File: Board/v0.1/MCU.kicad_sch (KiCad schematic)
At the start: 27 parts, among them J1 Conn_01x06_Male, SW1 RST_BTN, SW2 SCREEN_OFF_BTN, U1 ESP32-WROOM-32

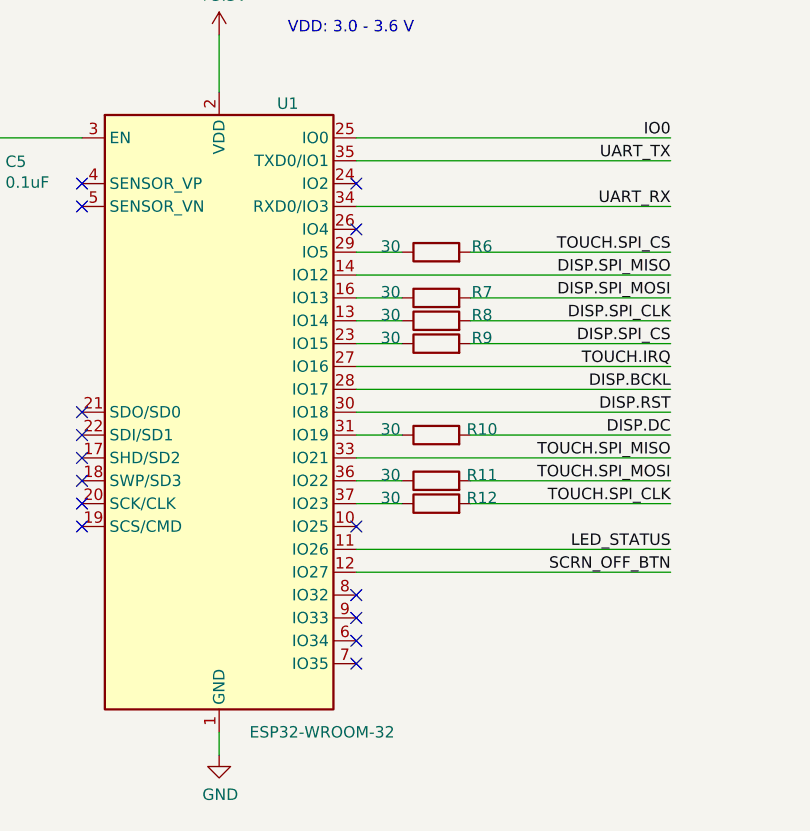
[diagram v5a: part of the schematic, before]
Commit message: Add labels to unused pins
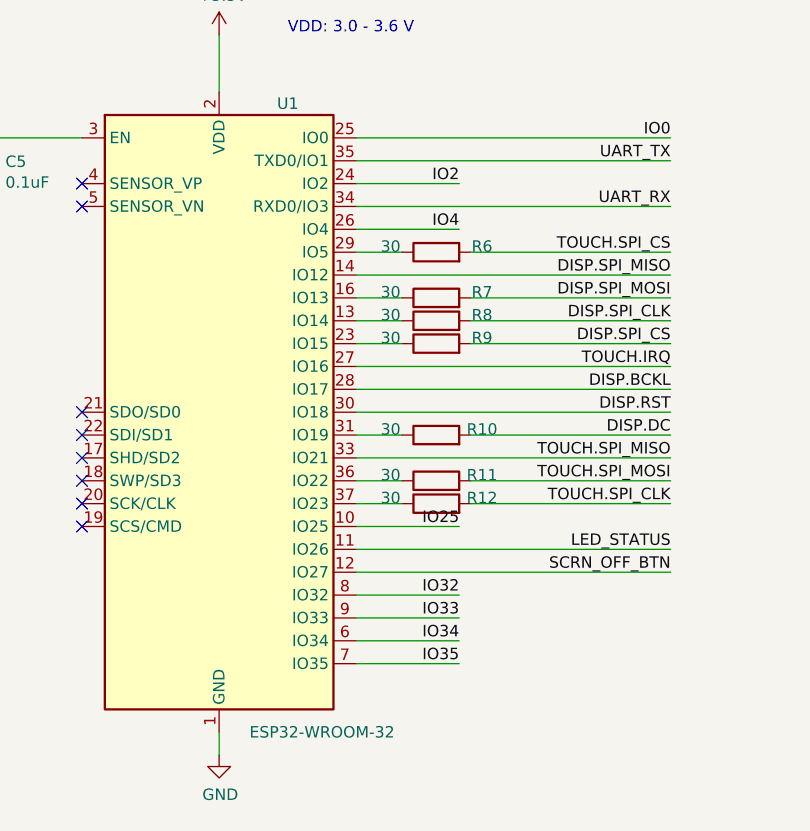
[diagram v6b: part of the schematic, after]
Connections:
- net IO25: now reaches U1.10 (IO25)
- net IO2: now reaches U1.24 (IO2)
- net IO4: now reaches U1.26 (IO4)
- net IO34: now reaches U1.6 (IO34)
- net IO35: now reaches U1.7 (IO35)
- net IO32: now reaches U1.8 (IO32)
- net IO33: now reaches U1.9 (IO33)
- no-connect marks 15 -> 8
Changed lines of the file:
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@@
   (no_connect (at 125.73 97.79))
   (no_connect (at 125.73 95.25))
-  (no_connect (at 156.21 115.57))
-  (no_connect (at 156.21 118.11))
   (no_connect (at 125.73 67.31))
-  (no_connect (at 156.21 113.03))
   (no_connect (at 125.73 100.33))
-  (no_connect (at 156.21 64.77))
-  (no_connect (at 156.21 102.87))
-  (no_connect (at 156.21 69.85))
   (no_connect (at 125.73 90.17))
   (no_connect (at 125.73 64.77))
   (no_connect (at 125.73 92.71))
-  (no_connect (at 156.21 110.49))
   (no_connect (at 125.73 102.87))
   (bus_entry (at 245.11 60.96) (size 2.54 2.54)
@@
     (stroke (width 0) (type default) (color 0 0 0 0))
   )
+  (wire (pts (xy 156.21 69.85) (xy 167.64 69.85))
+    (stroke (width 0) (type default) (color 0 0 0 0))
+  )
   (wire (pts (xy 99.06 59.69) (xy 104.14 59.69))
     (stroke (width 0) (type default) (color 0 0 0 0))
@@
     (stroke (width 0) (type default) (color 0 0 0 0))
   )
+  (wire (pts (xy 156.21 118.11) (xy 167.64 118.11))
+    (stroke (width 0) (type default) (color 0 0 0 0))
+  )
   (wire (pts (xy 228.6 63.5) (xy 245.11 63.5))
     (stroke (width 0) (type default) (color 0 0 0 0))
@@
     (stroke (width 0) (type default) (color 0 0 0 0))
   )
+  (wire (pts (xy 156.21 64.77) (xy 167.64 64.77))
+    (stroke (width 0) (type default) (color 0 0 0 0))
+  )
   (wire (pts (xy 60.96 177.8) (xy 60.96 179.705))
     (stroke (width 0) (type default) (color 0 0 0 0))
@@
     (stroke (width 0) (type default) (color 0 0 0 0))
   )
+  (wire (pts (xy 156.21 110.49) (xy 167.64 110.49))
+    (stroke (width 0) (type default) (color 0 0 0 0))
+  )
   (wire (pts (xy 156.21 80.01) (xy 161.29 80.01))
     (stroke (width 0) (type default) (color 0 0 0 0))
@@
     (stroke (width 0) (type default) (color 0 0 0 0))
   )
+  (wire (pts (xy 156.21 115.57) (xy 167.64 115.57))
+    (stroke (width 0) (type default) (color 0 0 0 0))
+  )
   (wire (pts (xy 268.605 147.955) (xy 261.62 147.955))
     (stroke (width 0) (type default) (color 0 0 0 0))
   )
+  (wire (pts (xy 156.21 113.03) (xy 167.64 113.03))
+    (stroke (width 0) (type default) (color 0 0 0 0))
+  )
   (wire (pts (xy 156.21 59.69) (xy 191.135 59.69))
     (stroke (width 0) (type default) (color 0 0 0 0))
@@
   )
   (wire (pts (xy 60.96 167.64) (xy 62.865 167.64))
+    (stroke (width 0) (type default) (color 0 0 0 0))
+  )
+  (wire (pts (xy 156.21 102.87) (xy 167.64 102.87))
     (stroke (width 0) (type default) (color 0 0 0 0))
   )
@@
     (effects (font (size 1.27 1.27)) (justify right bottom))
   )
+  (label "IO25" (at 167.64 102.87 180)
+    (effects (font (size 1.27 1.27)) (justify right bottom))
+  )
   (label "DISP.BCKL" (at 191.135 87.63 180)
     (effects (font (size 1.27 1.27)) (justify right bottom))
   )
+  (label "IO33" (at 167.64 113.03 180)
+    (effects (font (size 1.27 1.27)) (justify right bottom))
+  )
   (label "DISP.SPI_CS" (at 228.6 39.37 0)
     (effects (font (size 1.27 1.27)) (justify left bottom))
@@
     (effects (font (size 1.27 1.27)) (justify right bottom))
   )
+  (label "IO34" (at 167.64 115.57 180)
+    (effects (font (size 1.27 1.27)) (justify right bottom))
+  )
   (label "TOUCH.SPI_MISO" (at 228.6 58.42 0)
     (effects (font (size 1.27 1.27)) (justify left bottom))
@@
     (effects (font (size 1.27 1.27)) (justify right bottom))
   )
+  (label "IO35" (at 167.64 118.11 180)
+    (effects (font (size 1.27 1.27)) (justify right bottom))
+  )
   (label "TOUCH.SPI_MOSI" (at 228.6 60.96 0)
     (effects (font (size 1.27 1.27)) (justify left bottom))
@@
     (effects (font (size 1.27 1.27)) (justify left bottom))
   )
+  (label "IO2" (at 167.64 64.77 180)
+    (effects (font (size 1.27 1.27)) (justify right bottom))
+  )
   (label "UART_RX" (at 240.03 140.335 0)
     (effects (font (size 1.27 1.27)) (justify left bottom))
@@
     (effects (font (size 1.27 1.27)) (justify right bottom))
   )
+  (label "IO4" (at 167.64 69.85 180)
+    (effects (font (size 1.27 1.27)) (justify right bottom))
+  )
   (label "SCRN_OFF_BTN" (at 191.135 107.95 180)
     (effects (font (size 1.27 1.27)) (justify right bottom))
   )
+  (label "IO32" (at 167.64 110.49 180)
+    (effects (font (size 1.27 1.27)) (justify right bottom))
+  )
